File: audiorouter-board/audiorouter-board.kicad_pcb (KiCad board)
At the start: 2 copper layers, 199.4 x 100.3 mm, 117 parts, among them J1 Input_Ribbon_Connector, J2 Output_Ribbon_Connector, K1 FINDER-30.22, K10 FINDER-30.22, K11 FINDER-30.22, K12 FINDER-30.22, K13 FINDER-30.22, K14 FINDER-30.22, K15 FINDER-30.22, K16 FINDER-30.22, K17 FINDER-30.22, K18 FINDER-30.22, K19 FINDER-30.22, K2 FINDER-30.22, K20 FINDER-30.22, K21 FINDER-30.22, K22 FINDER-30.22, K23 FINDER-30.22, K24 FINDER-30.22, K3 FINDER-30.22, K4 FINDER-30.22, K5 FINDER-30.22, K6 FINDER-30.22, K7 FINDER-30.22, K8 FINDER-30.22, K9 FINDER-30.22, Q1 PN2222A, Q10 PN2222A, Q11 PN2222A, Q12 PN2222A, Q13 PN2222A, Q14 PN2222A, Q15 PN2222A, Q16 PN2222A, Q17 PN2222A, Q18 PN2222A, Q19 PN2222A, Q2 PN2222A, Q20 PN2222A, Q21 PN2222A, Q22 PN2222A, Q23 PN2222A, Q24 PN2222A, Q25 PN2222A, Q3 PN2222A, Q4 PN2222A, Q5 PN2222A, Q6 PN2222A, Q7 PN2222A, Q8 PN2222A, Q9 PN2222A, U1 74HC595, U2 74HC595, U3 74HC595, U4 L7805

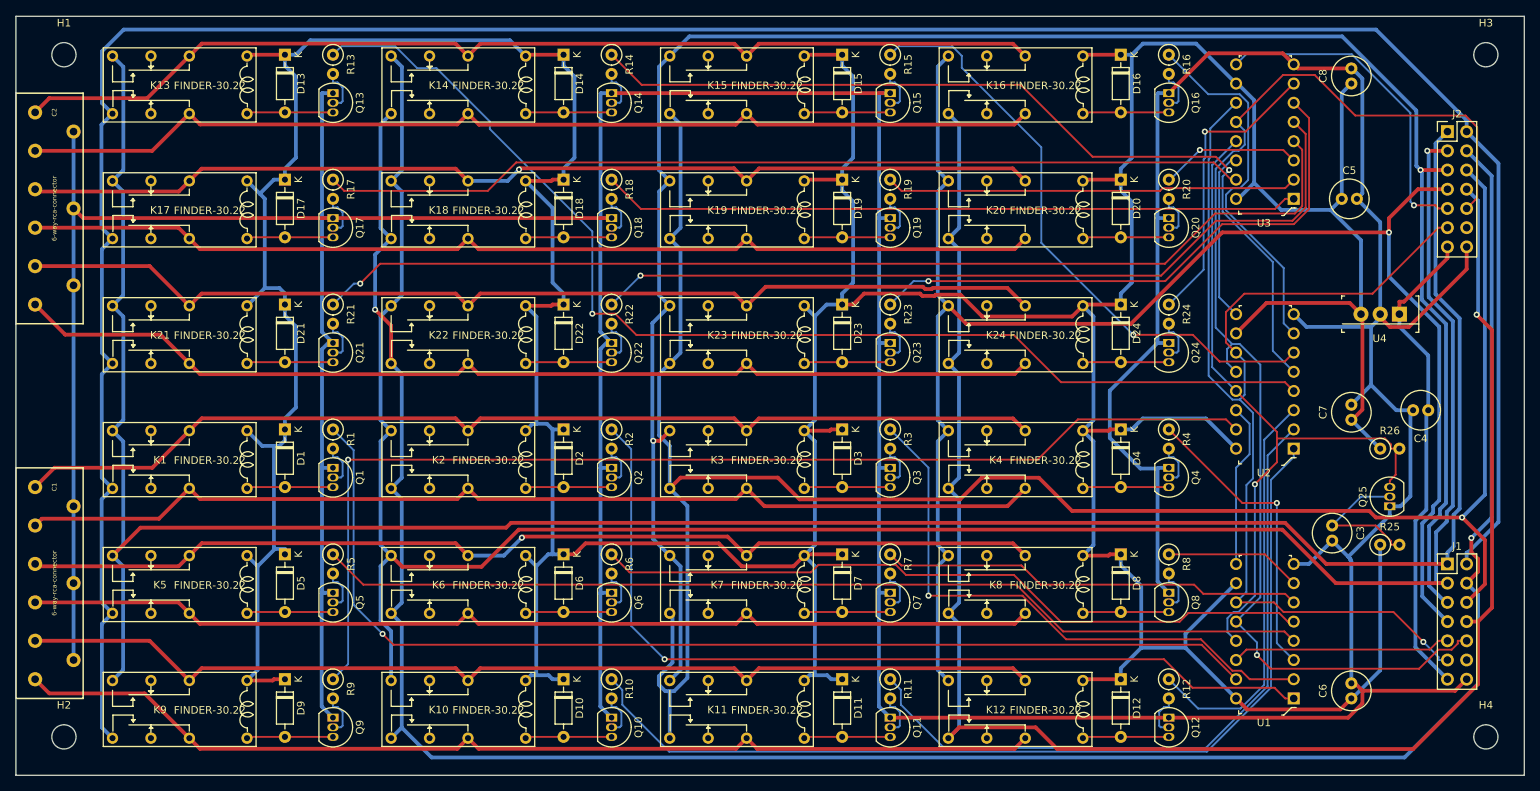
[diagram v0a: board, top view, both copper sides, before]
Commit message: Turned out that time delay circut for 595 output enable pins was bad idea in practice. I reworked my device by removing timed pull-down circuit components while leaving pull-up in place. Added wires to 12. pin both incoming and outgoing ribbon cables for pull-down from controller board. Added pulldown wire to controller.
Rewrote controller board arduino software for output enable logic.
Fixed bugs that caused parasitic powering of daughter boards via
595 data pins. Worked around noise induced false triggering by
overwriting correct state to 595 cascade every second. Added
software logic for drawn current limiting.
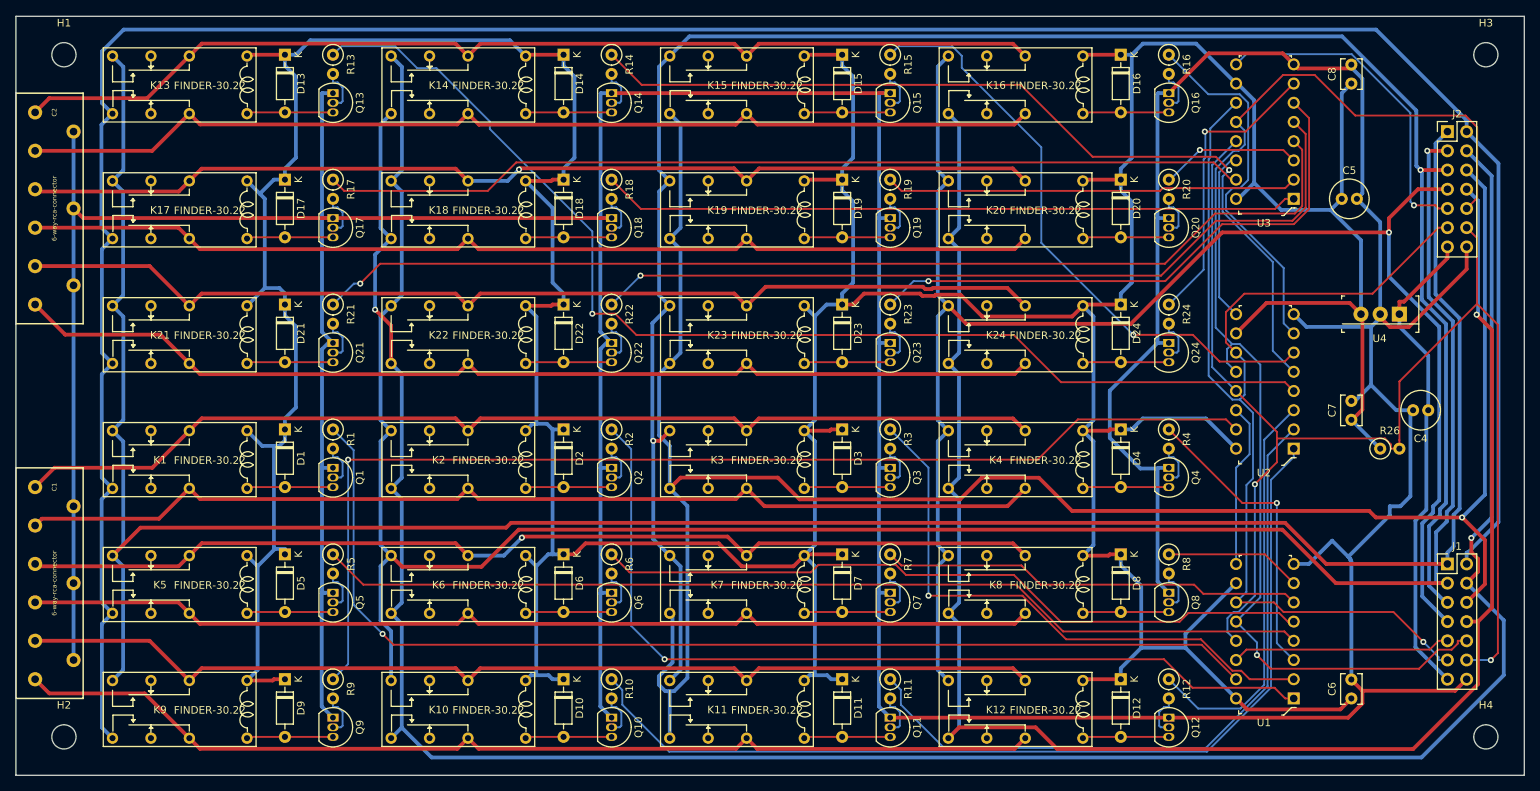
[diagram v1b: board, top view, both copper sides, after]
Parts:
- removed C3: 100u, Capacitor_THT:C_Radial_D5.0mm_H11.0mm_P2.00mm
- removed Q25: PN2222A, Package_TO_SOT_THT:TO-92_Inline
- removed R25: 220k, Resistor_THT:R_Axial_DIN0207_L6.3mm_D2.5mm_P2.54mm_Vertical
- C6, C7, C8: footprint Capacitor_THT:C_Radial_D5.0mm_H11.0mm_P2.00mm -> Capacitor_THT:C_Disc_D3.8mm_W2.6mm_P2.50mm
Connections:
- J1 pad 12: (no net) -> OutPutEnable
- J2 pad 12: (no net) -> OutPutEnable
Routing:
- net OutPutEnable: track 96.9 -> 177.4 mm, vias 1 -> 2
- net VCC: track 773.3 -> 751.4 mm
- net Net-(C3-Pad1): track 19.4 -> 0.00 mm
- net bus_2_R: track 311.5 -> 315.6 mm
